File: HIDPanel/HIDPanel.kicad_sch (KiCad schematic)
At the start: 47 parts, among them J1 2PosTerminal, M1 ModulePlug, M10 ModulePlug, M11 ModulePlug, M12 ModulePlug, M13 ModulePlug, M14 ModulePlug, M15 ModulePlug, M2 ModulePlug, M3 ModulePlug, M4 ModulePlug, M5 ModulePlug, M6 ModulePlug, M7 ModulePlug, M8 ModulePlug, M9 ModulePlug, Q1 2N3904, U1 Pico, U2 74HCT08, U3 4051, U4 4051, U5 4051, U6 TL431LP

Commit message: Tweaked some distances
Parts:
- renumbered M3 to M1, M9 to M11, M15 to M13, M13 to M15, M1 to M3, M7 to M5, M5 to M7, M11 to M9
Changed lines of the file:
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@@
   (symbol (lib_name "ModulePlug_11") (lib_id "ModulePlug:ModulePlug") (at 84.455 180.975 0) (unit 1)
     (in_bom yes) (on_board yes)
-    (property "Reference" "M3" (id 0) (at 83.185 177.8 0)
+    (property "Reference" "M1" (id 0) (at 83.185 177.8 0)
       (effects (font (size 1.27 1.27)) (justify left))
     )
@@
   (symbol (lib_name "ModulePlug_4") (lib_id "ModulePlug:ModulePlug") (at 107.95 101.6 0) (unit 1)
     (in_bom yes) (on_board yes)
-    (property "Reference" "M5" (id 0) (at 106.68 98.425 0)
+    (property "Reference" "M7" (id 0) (at 106.68 98.425 0)
       (effects (font (size 1.27 1.27)) (justify left))
     )
@@
   (symbol (lib_name "ModulePlug_8") (lib_id "ModulePlug:ModulePlug") (at 157.48 101.6 0) (unit 1)
     (in_bom yes) (on_board yes)
-    (property "Reference" "M13" (id 0) (at 156.21 98.425 0)
+    (property "Reference" "M15" (id 0) (at 156.21 98.425 0)
       (effects (font (size 1.27 1.27)) (justify left))
     )
@@
   (symbol (lib_name "ModulePlug_6") (lib_id "ModulePlug:ModulePlug") (at 83.185 101.6 0) (unit 1)
     (in_bom yes) (on_board yes)
-    (property "Reference" "M1" (id 0) (at 81.915 98.425 0)
+    (property "Reference" "M3" (id 0) (at 81.915 98.425 0)
       (effects (font (size 1.27 1.27)) (justify left))
     )
@@
   (symbol (lib_name "ModulePlug_9") (lib_id "ModulePlug:ModulePlug") (at 133.35 101.6 0) (unit 1)
     (in_bom yes) (on_board yes)
-    (property "Reference" "M9" (id 0) (at 132.08 98.425 0)
+    (property "Reference" "M11" (id 0) (at 132.08 98.425 0)
       (effects (font (size 1.27 1.27)) (justify left))
     )
@@
   (symbol (lib_name "ModulePlug_2") (lib_id "ModulePlug:ModulePlug") (at 160.655 180.975 0) (unit 1)
     (in_bom yes) (on_board yes)
-    (property "Reference" "M15" (id 0) (at 159.385 177.8 0)
+    (property "Reference" "M13" (id 0) (at 159.385 177.8 0)
       (effects (font (size 1.27 1.27)) (justify left))
     )
@@
   (symbol (lib_name "ModulePlug_13") (lib_id "ModulePlug:ModulePlug") (at 135.89 180.34 0) (unit 1)
     (in_bom yes) (on_board yes)
-    (property "Reference" "M11" (id 0) (at 134.62 177.165 0)
+    (property "Reference" "M9" (id 0) (at 134.62 177.165 0)
       (effects (font (size 1.27 1.27)) (justify left))
     )
@@
   (symbol (lib_name "ModulePlug_10") (lib_id "ModulePlug:ModulePlug") (at 109.855 180.34 0) (unit 1)
     (in_bom yes) (on_board yes)
-    (property "Reference" "M7" (id 0) (at 108.585 177.165 0)
+    (property "Reference" "M5" (id 0) (at 108.585 177.165 0)
       (effects (font (size 1.27 1.27)) (justify left))
     )
@@
       (reference "J1") (unit 1) (value "2PosTerminal") (footprint "TerminalBlock:TerminalBlock_bornier-2_P5.08mm")
     )
-    (path "/510b6617-315b-4c87-a6be-fc24bec8af70"
+    (path "/1ec98f11-002b-4940-a7f4-63f9c2c7b185"
       (reference "M1") (unit 1) (value "ModulePlug") (footprint "HIDPanel:ModulePlug")
     )
@@
       (reference "M2") (unit 1) (value "ModulePlug") (footprint "HIDPanel:ModulePlug")
     )
-    (path "/1ec98f11-002b-4940-a7f4-63f9c2c7b185"
+    (path "/510b6617-315b-4c87-a6be-fc24bec8af70"
       (reference "M3") (unit 1) (value "ModulePlug") (footprint "HIDPanel:ModulePlug")
     )
@@
       (reference "M4") (unit 1) (value "ModulePlug") (footprint "HIDPanel:ModulePlug")
     )
-    (path "/460f4bc0-4085-4e48-bf16-e170201dd44c"
+    (path "/bb26dc0c-e42d-4466-bf87-a95a89397101"
       (reference "M5") (unit 1) (value "ModulePlug") (footprint "HIDPanel:ModulePlug")
     )
@@
       (reference "M6") (unit 1) (value "ModulePlug") (footprint "HIDPanel:ModulePlug")
     )
-    (path "/bb26dc0c-e42d-4466-bf87-a95a89397101"
+    (path "/460f4bc0-4085-4e48-bf16-e170201dd44c"
       (reference "M7") (unit 1) (value "ModulePlug") (footprint "HIDPanel:ModulePlug")
     )
@@
       (reference "M8") (unit 1) (value "ModulePlug") (footprint "HIDPanel:ModulePlug")
     )
-    (path "/7a3becce-62e0-4bd9-8d92-fa36498b7f8c"
+    (path "/a582a128-beec-4f1f-9d82-230c8222ebe1"
       (reference "M9") (unit 1) (value "ModulePlug") (footprint "HIDPanel:ModulePlug")
     )
@@
       (reference "M10") (unit 1) (value "ModulePlug") (footprint "HIDPanel:ModulePlug")
     )
-    (path "/a582a128-beec-4f1f-9d82-230c8222ebe1"
+    (path "/7a3becce-62e0-4bd9-8d92-fa36498b7f8c"
       (reference "M11") (unit 1) (value "ModulePlug") (footprint "HIDPanel:ModulePlug")
     )
@@
       (reference "M12") (unit 1) (value "ModulePlug") (footprint "HIDPanel:ModulePlug")
     )
-    (path "/47e7b1d9-245a-4b16-bf74-21ad8f480ef8"
+    (path "/96597706-4b45-4f39-918d-c9c738cfbc5f"
       (reference "M13") (unit 1) (value "ModulePlug") (footprint "HIDPanel:ModulePlug")
     )
@@
       (reference "M14") (unit 1) (value "ModulePlug") (footprint "HIDPanel:ModulePlug")
     )
-    (path "/96597706-4b45-4f39-918d-c9c738cfbc5f"
+    (path "/47e7b1d9-245a-4b16-bf74-21ad8f480ef8"
       (reference "M15") (unit 1) (value "ModulePlug") (footprint "HIDPanel:ModulePlug")
     )

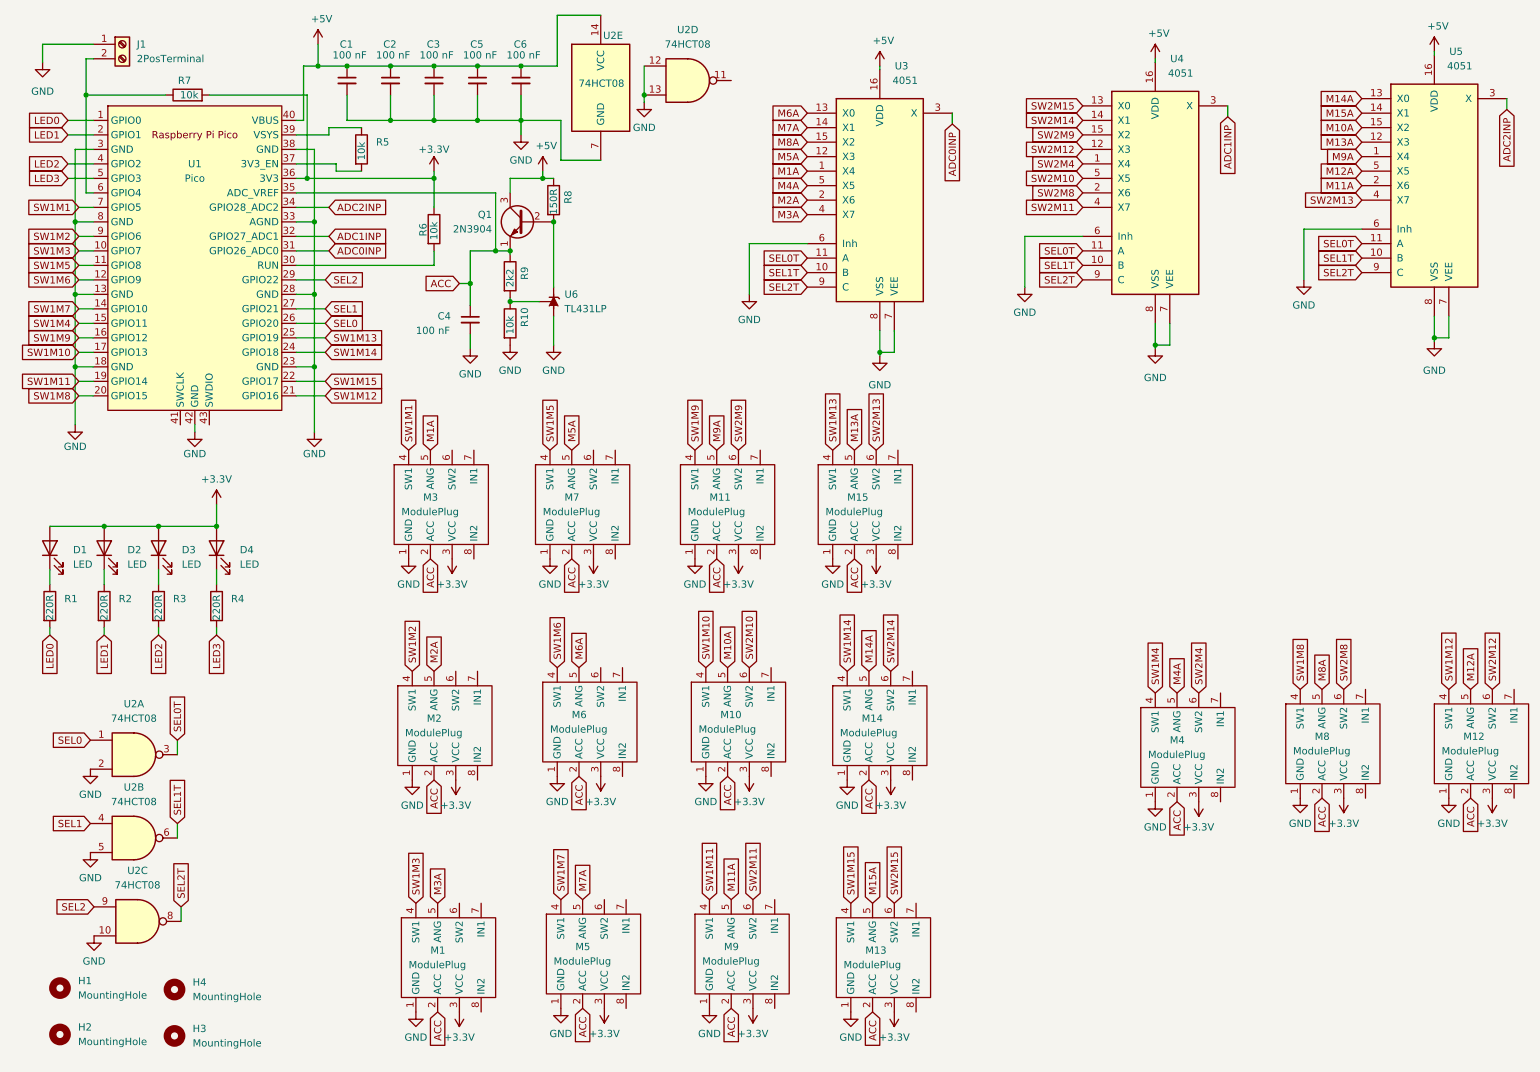
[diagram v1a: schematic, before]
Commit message: Oops 74HCT32 not 74HCT08
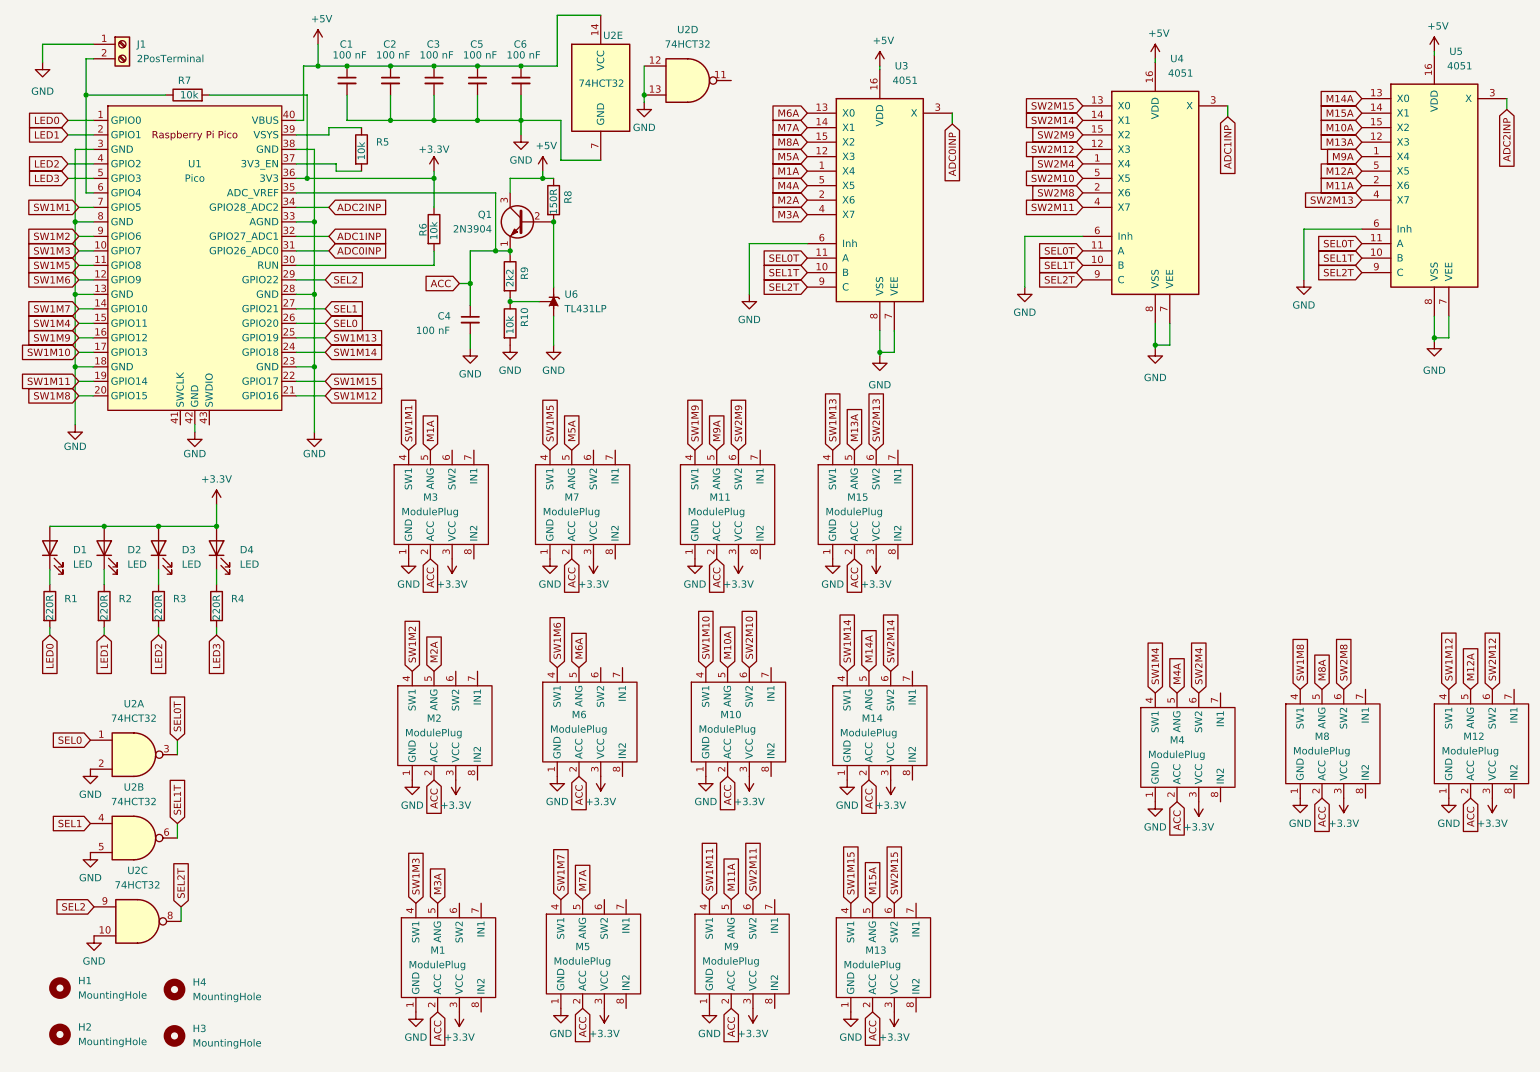
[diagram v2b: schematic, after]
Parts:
- U2: value 74HCT08 -> 74HCT32
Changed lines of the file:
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@@
     (in_bom yes) (on_board yes) (fields_autoplaced)
     (property "Reference" "U2" (id 0) (at 31.877 163.83 0))
-    (property "Value" "74HCT08" (id 1) (at 31.877 166.37 0))
+    (property "Value" "74HCT32" (id 1) (at 31.877 166.37 0))
     (property "Footprint" "Package_DIP:DIP-14_W7.62mm_Socket" (id 2) (at 31.877 172.72 0)
       (effects (font (size 1.27 1.27)) hide)
@@
     (in_bom yes) (on_board yes) (fields_autoplaced)
     (property "Reference" "U2" (id 0) (at 31.242 134.62 0))
-    (property "Value" "74HCT08" (id 1) (at 31.242 137.16 0))
+    (property "Value" "74HCT32" (id 1) (at 31.242 137.16 0))
     (property "Footprint" "Package_DIP:DIP-14_W7.62mm_Socket" (id 2) (at 31.242 143.51 0)
       (effects (font (size 1.27 1.27)) hide)
@@
     (in_bom yes) (on_board yes)
     (property "Reference" "U2" (id 0) (at 115.189 17.526 0))
-    (property "Value" "74HCT08" (id 1) (at 113.157 25.908 0))
+    (property "Value" "74HCT32" (id 1) (at 113.157 25.908 0))
     (property "Footprint" "Package_DIP:DIP-14_W7.62mm_Socket" (id 2) (at 113.03 26.67 0)
       (effects (font (size 1.27 1.27)) hide)
@@
     (in_bom yes) (on_board yes) (fields_autoplaced)
     (property "Reference" "U2" (id 0) (at 128.27 16.51 0))
-    (property "Value" "74HCT08" (id 1) (at 128.27 19.05 0))
+    (property "Value" "74HCT32" (id 1) (at 128.27 19.05 0))
     (property "Footprint" "Package_DIP:DIP-14_W7.62mm_Socket" (id 2) (at 128.27 25.4 0)
       (effects (font (size 1.27 1.27)) hide)
@@
     (in_bom yes) (on_board yes) (fields_autoplaced)
     (property "Reference" "U2" (id 0) (at 31.242 149.225 0))
-    (property "Value" "74HCT08" (id 1) (at 31.242 151.765 0))
+    (property "Value" "74HCT32" (id 1) (at 31.242 151.765 0))
     (property "Footprint" "Package_DIP:DIP-14_W7.62mm_Socket" (id 2) (at 31.242 158.115 0)
       (effects (font (size 1.27 1.27)) hide)
@@
     )
     (path "/7eb8a954-00f4-42dc-b8b1-2c08caa3c534"
-      (reference "U2") (unit 1) (value "74HCT08") (footprint "Package_DIP:DIP-14_W7.62mm_Socket")
+      (reference "U2") (unit 1) (value "74HCT32") (footprint "Package_DIP:DIP-14_W7.62mm_Socket")
     )
     (path "/db963f7e-7562-485d-8d5e-6ab173a171e7"
-      (reference "U2") (unit 2) (value "74HCT08") (footprint "Package_DIP:DIP-14_W7.62mm_Socket")
+      (reference "U2") (unit 2) (value "74HCT32") (footprint "Package_DIP:DIP-14_W7.62mm_Socket")
     )
     (path "/3b90c152-9e90-48d9-8f22-8de3c8ee7885"
-      (reference "U2") (unit 3) (value "74HCT08") (footprint "Package_DIP:DIP-14_W7.62mm_Socket")
+      (reference "U2") (unit 3) (value "74HCT32") (footprint "Package_DIP:DIP-14_W7.62mm_Socket")
     )
     (path "/d8ee3a1e-2b26-43cd-884d-67bff2468fdb"
-      (reference "U2") (unit 4) (value "74HCT08") (footprint "Package_DIP:DIP-14_W7.62mm_Socket")
+      (reference "U2") (unit 4) (value "74HCT32") (footprint "Package_DIP:DIP-14_W7.62mm_Socket")
     )
     (path "/8b77a2f1-610b-46da-8ee0-866eaaee6a07"
-      (reference "U2") (unit 5) (value "74HCT08") (footprint "Package_DIP:DIP-14_W7.62mm_Socket")
+      (reference "U2") (unit 5) (value "74HCT32") (footprint "Package_DIP:DIP-14_W7.62mm_Socket")
     )
     (path "/977f8a8e-d10b-4629-baae-a76a4d019b7b"

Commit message: Rev 2 HIDPanel board
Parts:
- added JP1: Jumper_3_Bridged12, Jumper:SolderJumper-3_P1.3mm_Bridged2Bar12_Pad1.0x1.5mm, symbol Jumper:Jumper_3_Bridged12
- J1: footprint TerminalBlock:TerminalBlock_bornier-2_P5.08mm -> Connector_PinHeader_2.54mm:PinHeader_1x02_P2.54mm_Vertical
- U2: value 74HCT32 -> 74HCT00
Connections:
- net +5V: now also JP1.1 (A)
- net GND: now also JP1.3 (B); no longer U2.10, U2.2, U2.5
- new net: JP1.2 (C), U2.10, U2.2, U2.5
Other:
- moved on the sheet: H1, H2, H3, H4
